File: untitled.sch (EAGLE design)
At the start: 25 parts

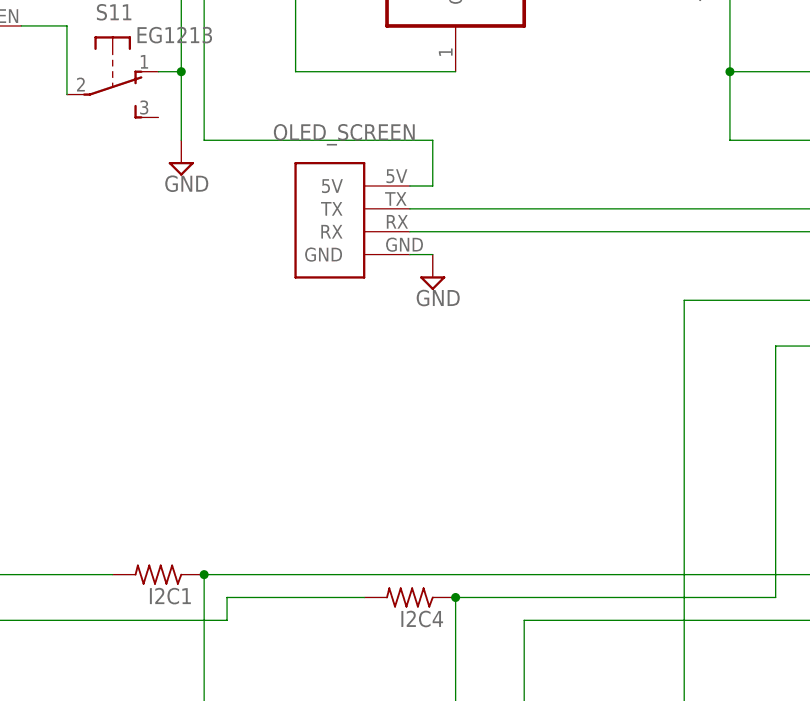
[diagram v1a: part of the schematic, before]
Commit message: added optional speaker
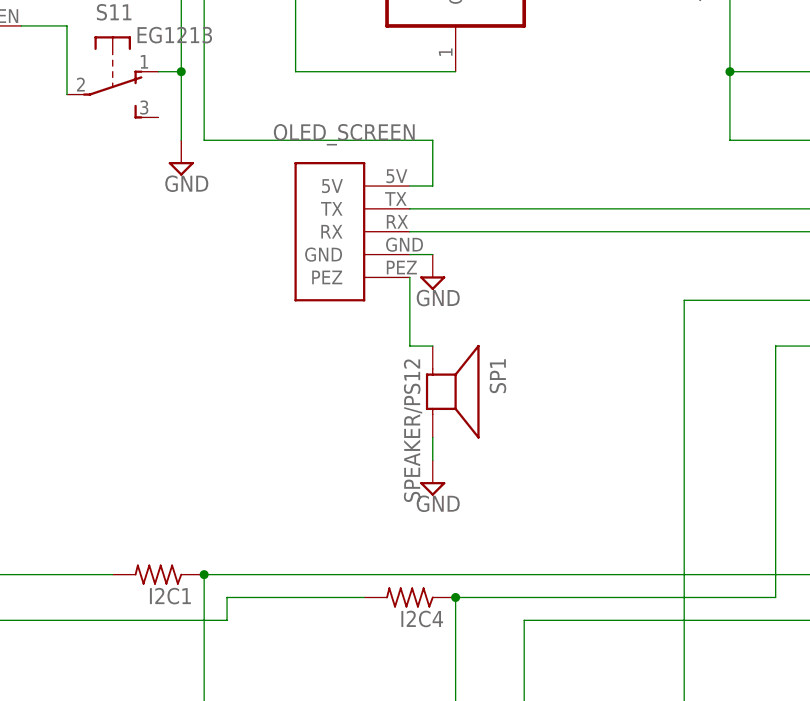
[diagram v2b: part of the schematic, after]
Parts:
- added SP1: SPEAKER/PS12, adafruit:SPEAKER/PS12
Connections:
- new net N$12: OLED_SCREEN.PEZ, SP1.+
- net GND: now also SP1.-
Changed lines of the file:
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@@
 <part name="+3V9" library="supply1" deviceset="+3V3" device=""/>
 <part name="3.3LDO" library="burr-brown" deviceset="REG1117" device="X"/>
+<part name="SP1" library="adafruit" deviceset="SPEAKER" device="/PS12"/>
+<part name="SUPPLY10" library="supply2" deviceset="GND" device=""/>
 </parts>
 <sheets>
@@
 <instance part="+3V9" gate="G$1" x="-7.62" y="25.4"/>
 <instance part="3.3LDO" gate="G$1" x="-55.88" y="96.52"/>
+<instance part="SP1" gate="S1" x="-58.42" y="48.26" rot="R270"/>
+<instance part="SUPPLY10" gate="GND" x="-58.42" y="38.1"/>
 </instances>
 <busses>
@@
 <wire x1="-7.62" y1="12.7" x2="-7.62" y2="10.16" width="0.1524" layer="91"/>
 </segment>
+<segment>
+<pinref part="SUPPLY10" gate="GND" pin="GND"/>
+<pinref part="SP1" gate="S1" pin="-"/>
+<wire x1="-58.42" y1="40.64" x2="-58.42" y2="43.18" width="0.1524" layer="91"/>
+</segment>
 </net>
 <net name="+5V" class="0">
@@
 </segment>
 </net>
+<net name="N$12" class="0">
+<segment>
+<pinref part="OLED_SCREEN" gate="G$1" pin="PEZ"/>
+<wire x1="-60.96" y1="60.96" x2="-60.96" y2="53.34" width="0.1524" layer="91"/>
+<pinref part="SP1" gate="S1" pin="+"/>
+<wire x1="-60.96" y1="53.34" x2="-58.42" y2="53.34" width="0.1524" layer="91"/>
+</segment>
+</net>
